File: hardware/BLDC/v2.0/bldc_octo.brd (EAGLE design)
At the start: 60 x 60 mm, 5 parts, among them J1 PWR_2_XT30PW-M, J2 LINEAR_3_MOLEX_5023520300, J3 LINEAR_3_AMASS_MR30PW-M, U1 MA702, U2 STM32H723VGT6

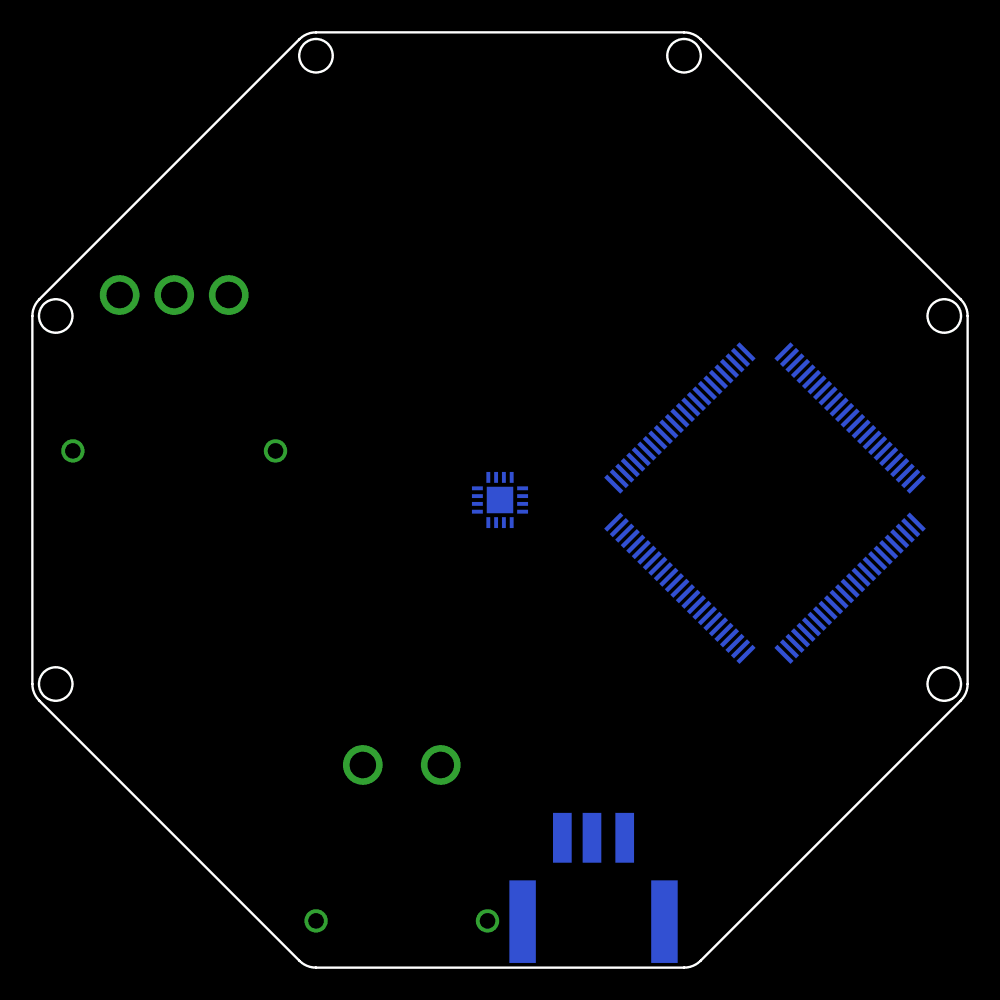
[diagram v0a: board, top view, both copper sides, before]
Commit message: Added drv and 24MHz crystal
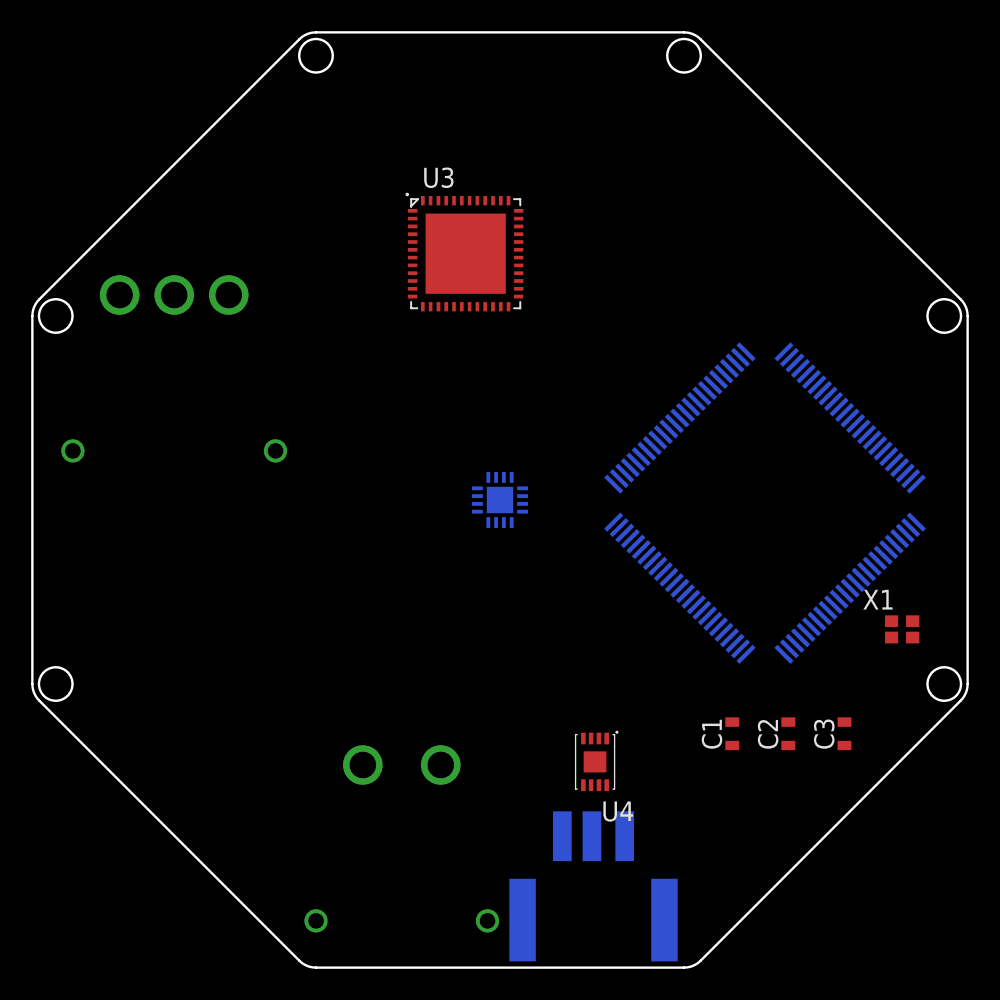
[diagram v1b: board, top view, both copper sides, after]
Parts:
- added C1: (no value), _T_rcl:C0603
- added C2, C3: 10pf 10V, _T_rcl:C0603
- added U3: DRV8323RS, _T_ic:VQFN-48_7X7
- added U4: MCP2542FD, _T_ic:TDFN_2X3
- added X1: CRYSTAL_NX2016SA-24MHZ-EXS00A-CS11335, _T_ic:NX201SA
- moved J2 0.10 mm to (36.0, 0.30)
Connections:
- new net +24V: J1.P$2
- new net GND: C1.2, C2.2, C3.2, J1.P$1, J2.P$3, X1.P$2, X1.P$4
- new net N$1: J2.P$1, U4.7
- new net N$2: J2.P$2, U4.6
- new net N$3: C2.1, U2.13, X1.P$1
- new net N$4: C3.1, U2.12, X1.P$3
- new net NRST: C1.1, U2.14
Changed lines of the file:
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@@
 <attribute name="VALUE" x="33.2" y="26.85" locked="yes" size="1.27" layer="28" rot="MR0"/>
 </element>
-<element name="J2" library="_T_conn" library_urn="urn:adsk.eagle:library:19570503" package="MOLEX_5023520300" package3d_urn="urn:adsk.eagle:package:24616683/3" value="LINEAR_3_MOLEX_5023520300" x="36" y="0.2" smashed="yes" rot="MR0">
-<attribute name="NAME" x="36" y="3.54" size="0.8" layer="26" font="vector" rot="MR0" align="center"/>
-<attribute name="VALUE" x="36" y="2" size="0.8" layer="28" font="vector" rot="MR0" align="center"/>
+<element name="J2" library="_T_conn" library_urn="urn:adsk.eagle:library:19570503" package="MOLEX_5023520300" package3d_urn="urn:adsk.eagle:package:24616683/3" value="LINEAR_3_MOLEX_5023520300" x="36" y="0.3" smashed="yes" rot="MR0">
+<attribute name="NAME" x="36" y="3.64" size="0.8" layer="26" font="vector" rot="MR0" align="center"/>
+<attribute name="VALUE" x="36" y="2.1" size="0.8" layer="28" font="vector" rot="MR0" align="center"/>
 </element>
 <element name="J3" library="_T_conn" library_urn="urn:adsk.eagle:library:19570503" package="MR30PW-M" package3d_urn="urn:adsk.eagle:package:24615839/8" value="LINEAR_3_AMASS_MR30PW-M" x="9.1" y="33.15" smashed="yes" rot="MR0">
@@
 <attribute name="NAME" x="27.51" y="5.54" size="1.27" layer="26" rot="MR0"/>
 <attribute name="VALUE" x="27.51" y="1.73" size="1.27" layer="28" rot="MR0"/>
+</element>
+<element name="X1" library="_T_ic" library_urn="urn:adsk.eagle:library:19571245" package="NX201SA" package3d_urn="urn:adsk.eagle:package:19324209/4" value="CRYSTAL_NX2016SA-24MHZ-EXS00A-CS11335" x="55.8" y="21.7" smashed="yes">
+<attribute name="NAME" x="53.26" y="22.97" size="1.27" layer="25"/>
+<attribute name="VALUE" x="53.26" y="19.16" size="1.27" layer="27"/>
+</element>
+<element name="C1" library="_T_rcl" library_urn="urn:adsk.eagle:library:19571919" package="C0603" package3d_urn="urn:adsk.eagle:package:19572011/4" value="" x="44.9" y="15" smashed="yes" rot="R90">
+<attribute name="NAME" x="43.6" y="15" size="1.27" layer="25" rot="R90" align="center"/>
+<attribute name="VALUE" x="46.2" y="15" size="1.27" layer="27" rot="R90" align="center"/>
+</element>
+<element name="C2" library="_T_rcl" library_urn="urn:adsk.eagle:library:19571919" package="C0603" package3d_urn="urn:adsk.eagle:package:19572011/4" value="10pf 10V" x="48.5" y="15" smashed="yes" rot="R90">
+<attribute name="NAME" x="47.2" y="15" size="1.27" layer="25" rot="R90" align="center"/>
+<attribute name="VALUE" x="49.8" y="15" size="1.27" layer="27" rot="R90" align="center"/>
+</element>
+<element name="C3" library="_T_rcl" library_urn="urn:adsk.eagle:library:19571919" package="C0603" package3d_urn="urn:adsk.eagle:package:19572011/4" value="10pf 10V" x="52.1" y="15" smashed="yes" rot="R90">
+<attribute name="NAME" x="50.8" y="15" size="1.27" layer="25" rot="R90" align="center"/>
+<attribute name="VALUE" x="53.4" y="15" size="1.27" layer="27" rot="R90" align="center"/>
+</element>
+<element name="U3" library="_T_ic" library_urn="urn:adsk.eagle:library:19571245" package="VQFN-48_7X7" package3d_urn="urn:adsk.eagle:package:19571846/5" value="DRV8323RS" x="27.8" y="45.8" smashed="yes">
+<attribute name="DATASHEET" value="https://www.ti.com/lit/ds/symlink/drv8323r.pdf?ts=1587957100782" x="27.8" y="45.8" size="1.778" layer="27" display="off"/>
+<attribute name="NAME" x="25" y="50.04" size="1.27" layer="25"/>
+<attribute name="VALUE" x="24.5" y="40.45" size="1.27" layer="27"/>
+</element>
+<element name="U4" library="_T_ic" library_urn="urn:adsk.eagle:library:19571245" package="TDFN_2X3" package3d_urn="urn:adsk.eagle:package:19399098/4" value="MCP2542FD" x="36.1" y="13.2" smashed="yes" rot="R180">
+<attribute name="NAME" x="38.64" y="10.66" size="1.27" layer="25" rot="R180"/>
+<attribute name="VALUE" x="38.64" y="17.01" size="1.27" layer="27" rot="R180"/>
 </element>
 </elements>
@@
 <contactref element="U2" pad="20"/>
 </signal>
+<signal name="GND">
+<contactref element="C1" pad="2"/>
+<contactref element="C2" pad="2"/>
+<contactref element="X1" pad="P$2"/>
+<contactref element="X1" pad="P$4"/>
+<contactref element="C3" pad="2"/>
+<contactref element="J2" pad="P$3"/>
+<contactref element="J1" pad="P$1"/>
+<wire x1="55.125" y1="22.225" x2="56.475" y2="21.175" width="0" layer="19" extent="1-1"/>
+<wire x1="52.1" y1="14.25" x2="56.475" y2="21.175" width="0" layer="19" extent="1-1"/>
+<wire x1="48.5" y1="14.25" x2="52.1" y2="14.25" width="0" layer="19" extent="1-1"/>
+<wire x1="44.9" y1="14.25" x2="48.5" y2="14.25" width="0" layer="19" extent="1-1"/>
+<wire x1="34" y1="8.43" x2="44.9" y2="14.25" width="0" layer="19" extent="1-16"/>
+<wire x1="26.2" y1="13" x2="34" y2="8.43" width="0" layer="19" extent="16-16"/>
+</signal>
+<signal name="NRST">
+<contactref element="U2" pad="14"/>
+<contactref element="C1" pad="1"/>
+<wire x1="44.9" y1="15.75" x2="52.10644375" y2="23.98645" width="0" layer="19" extent="1-16"/>
+</signal>
+<signal name="N$3">
+<contactref element="U2" pad="13"/>
+<contactref element="C2" pad="1"/>
+<contactref element="X1" pad="P$1"/>
+<wire x1="55.125" y1="21.175" x2="52.459996875" y2="24.340003125" width="0" layer="19" extent="1-16"/>
+<wire x1="48.5" y1="15.75" x2="55.125" y2="21.175" width="0" layer="19" extent="1-1"/>
+</signal>
+<signal name="N$4">
+<contactref element="U2" pad="12"/>
+<contactref element="C3" pad="1"/>
+<contactref element="X1" pad="P$3"/>
+<wire x1="52.81355" y1="24.69355625" x2="56.475" y2="22.225" width="0" layer="19" extent="1-16"/>
+<wire x1="52.1" y1="15.75" x2="56.475" y2="22.225" width="0" layer="19" extent="1-1"/>
+</signal>
+<signal name="N$1">
+<contactref element="U4" pad="7"/>
+<contactref element="J2" pad="P$1"/>
+<wire x1="38" y1="8.43" x2="36.35" y2="11.7" width="0" layer="19" extent="1-16"/>
+</signal>
+<signal name="N$2">
+<contactref element="J2" pad="P$2"/>
+<contactref element="U4" pad="6"/>
+<wire x1="35.9" y1="8.43" x2="35.85" y2="11.7" width="0" layer="19" extent="1-16"/>
+</signal>
+<signal name="+24V">
+<contactref element="J1" pad="P$2"/>
+</signal>
 </signals>
